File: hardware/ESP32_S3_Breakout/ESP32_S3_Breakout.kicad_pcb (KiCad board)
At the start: 2 copper layers, 30.5 x 54.7 mm, 25 parts, among them J1 USB_C_Receptacle_USB2.0, J2 Conn_01x20_Pin, J3 Conn_01x20_Pin, Q1 2N7002DW, SW1 SW_DPDT_x2, SW2 RESET, SW3 BOOT, U1 ESP32-S3-WROOM, U2 USBLC6-2P6, U3 CH340G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

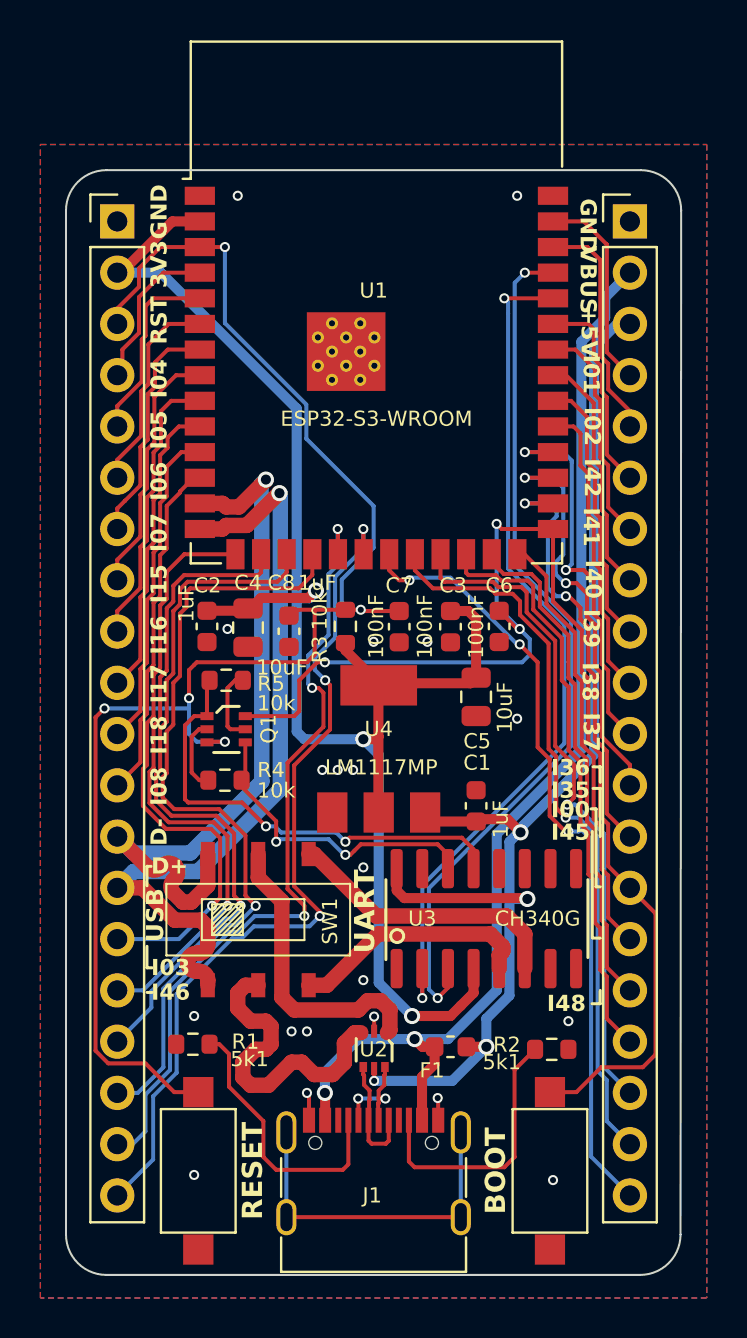
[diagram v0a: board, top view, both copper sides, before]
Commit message: Version 02 - Added LEDs
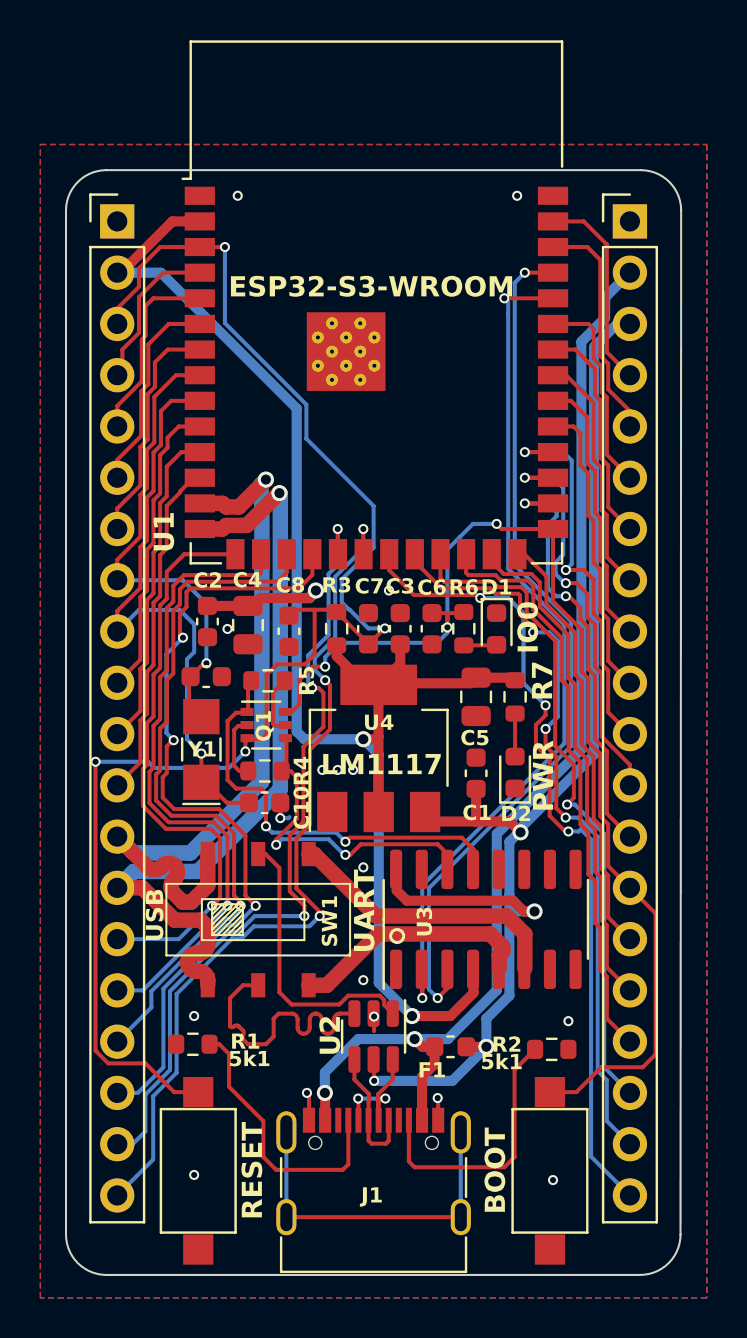
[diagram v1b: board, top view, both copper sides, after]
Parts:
- added C10: 12pF, Capacitor_SMD:C_0603_1608Metric, F.Cu at (148.3, 79.6)
- added C9: 12pF, Capacitor_SMD:C_0603_1608Metric, F.Cu at (145.4, 73.4)
- added D1: IO0, LED_SMD:LED_0603_1608Metric, F.Cu at (159.8, 71.0)
- added D2: PWR, LED_SMD:LED_0603_1608Metric, F.Cu at (160.7, 78.1)
- added R6: 1k, Resistor_SMD:R_0603_1608Metric, F.Cu at (158.1, 71.0)
- added R7: 1k, Resistor_SMD:R_0603_1608Metric, F.Cu at (160.7, 74.4)
- added Y1: 32.768kHz, Crystal:Crystal_SMD_EuroQuartz_EQ161-2Pin_3.2x1.5mm_HandSoldering, F.Cu at (145.1, 77.0)
- U2: value USBLC6-2P6 -> USBLC6-2SC6; footprint Package_TO_SOT_SMD:SOT-666 -> Package_TO_SOT_SMD:SOT-23-6
- U4: value LM1117MP -> LM1117
- moved C6 3.33 mm to (156.6, 71.0)
- moved C3 2.49 mm to (155.0, 71.0), turned to -90 degrees
- moved R5 2.07 mm to (148.4, 73.6)
- moved R4 2.03 mm to (148.3, 78.0)
- moved Q1 2.00 mm to (148.4, 75.8)
- moved C1 1.61 mm to (158.8, 78.1)
- moved C7 1.53 mm to (153.4, 71.0), turned to -90 degrees
- moved U2 0.66 mm to (153.7, 91.2)
- moved R3 0.45 mm to (151.8, 71.0)
- moved C2 0.24 mm to (145.4, 70.6)
- moved C4 0.13 mm to (147.4, 70.8)
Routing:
- net GPIO16: track 14.0 -> 29.6 mm, vias 0 -> 1
- net GPIO15: track 12.5 -> 23.7 mm, vias 0 -> 1
- net GPIO00: track 61.8 -> 57.0 mm
- net +5V: track 62.2 -> 64.7 mm
- net RST: track 77.8 -> 75.5 mm, vias 5 -> 4
- net Net-(D2-A): track 0.00 -> 2.13 mm
- net DTR: track 23.2 -> 21.4 mm
- net D-: track 5.56 -> 7.22 mm
- net Net-(D1-A): track 0.00 -> 1.64 mm
- net USB_DP: track 15.5 -> 13.9 mm
- net GPIO13: track 39.1 -> 40.4 mm
- net GND: track 3.04 -> 4.28 mm, vias 20 -> 17
- net GPIO14: track 36.2 -> 37.1 mm, vias 1 -> 3
- net USB_DN: track 14.8 -> 14.1 mm
- net +3V3: track 81.8 -> 82.5 mm
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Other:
- board text removed: "+5V"
